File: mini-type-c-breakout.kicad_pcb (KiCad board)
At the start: 2 copper layers, 11 parts, among them J0 TYPE-C-31-M12_13_EDITED, J1 ConnectionPoint, J2 ConnectionPoint, J3 ConnectionPoint, J4 ConnectionPoint, J5 ConnectionPoint, J6 ConnectionPoint, J7 ConnectionPoint, J8 ConnectionPoint

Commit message: v1.0a complete
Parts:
- removed J1, J2, J3, J4, J5, J6, J7, J8: ConnectionPoint, TestPoint:TestPoint_THTPad_1.0x1.0mm_Drill0.5mm
- added D+: Conn_01x01, TestPoint:TestPoint_Pad_1.0x1.0mm, F.Cu at (281.0, 163.6)
- added D-: Conn_01x01, TestPoint:TestPoint_Pad_1.0x1.0mm, F.Cu at (279.6, 163.6)
- added GND: Conn_01x01, TestPoint:TestPoint_Pad_1.0x1.0mm, F.Cu at (277.3, 163.6)
- added VCC: Conn_01x01, TestPoint:TestPoint_Pad_1.0x1.0mm, F.Cu at (283.3, 163.6)
- J0: footprint mini-general-tweaks:TYPE-C-31-M-12-No-SHIELD -> mini-general-tweaks:HRO-TYPE-C-No-SHIELD
- R0, R1: moved to B.Cu
- moved J0 47.6 mm to (280.3, 160.3)
- moved R0 38.2 mm to (278.2, 163.5)
- moved R1 35.3 mm to (282.5, 163.5), turned to 180 degrees
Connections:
- net CC1 renamed Net-(J0-Pad4)
- net CC2 renamed Net-(J0-Pad10)
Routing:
- net VCC: track 0.00 -> 11.1 mm, vias 0 -> 2
- net GND: track 0.00 -> 6.64 mm, vias 0 -> 2
- net Net-(J0-Pad4): track 0.00 -> 4.21 mm, vias 0 -> 1
- net Net-(J0-Pad10): track 0.00 -> 3.79 mm, vias 0 -> 1
- net USB_D+: track 5.05 -> 7.36 mm, vias 0 -> 2
- net USB_D-: track 6.85 -> 7.54 mm
- added copper zone on B.Cu, net GND
- added copper zone on F.Cu, net GND
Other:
- board outline added: 7.6 x 4.8 mm
- board text added: "Non-standard Type C Breakout Board"

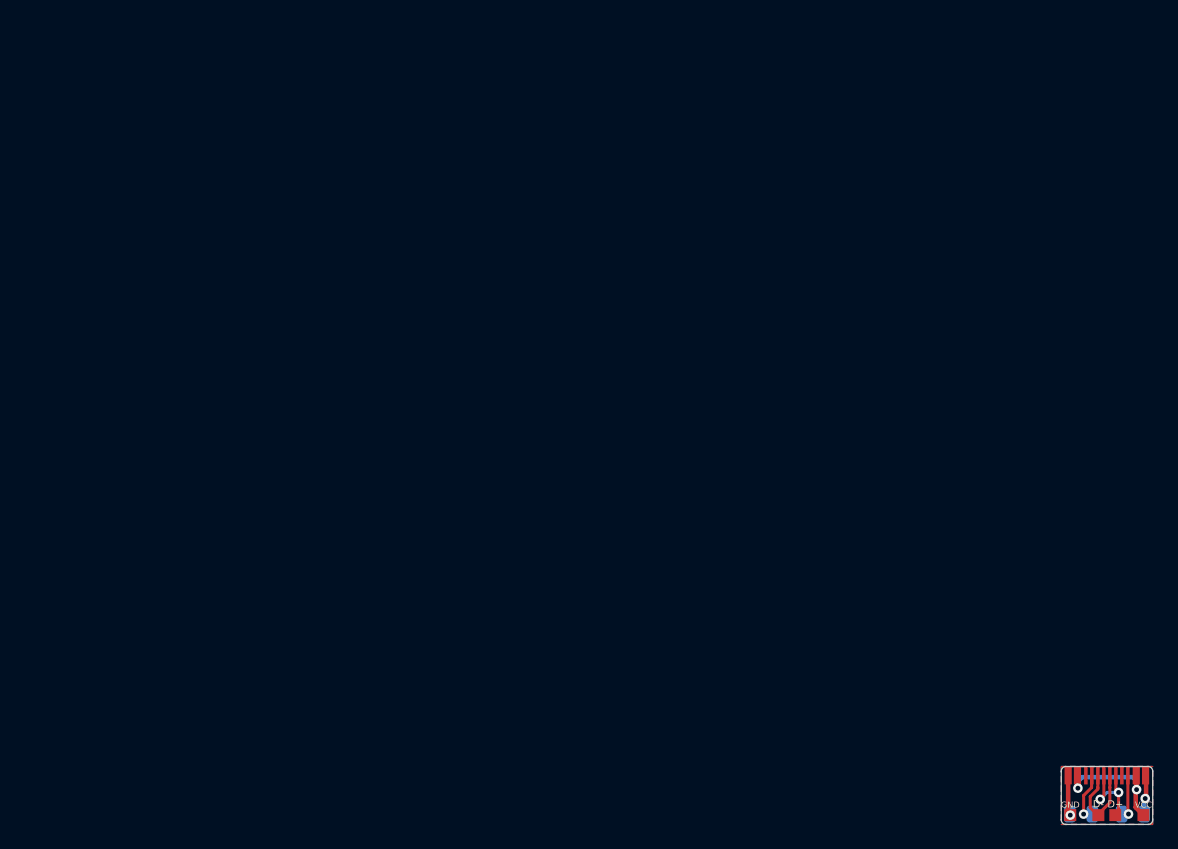
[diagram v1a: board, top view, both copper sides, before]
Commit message: Many tweaks, additions, etc.
Added licensing, tweaked PCB silkscreen, added logos to schematic, tweaked schematic layout, etc.
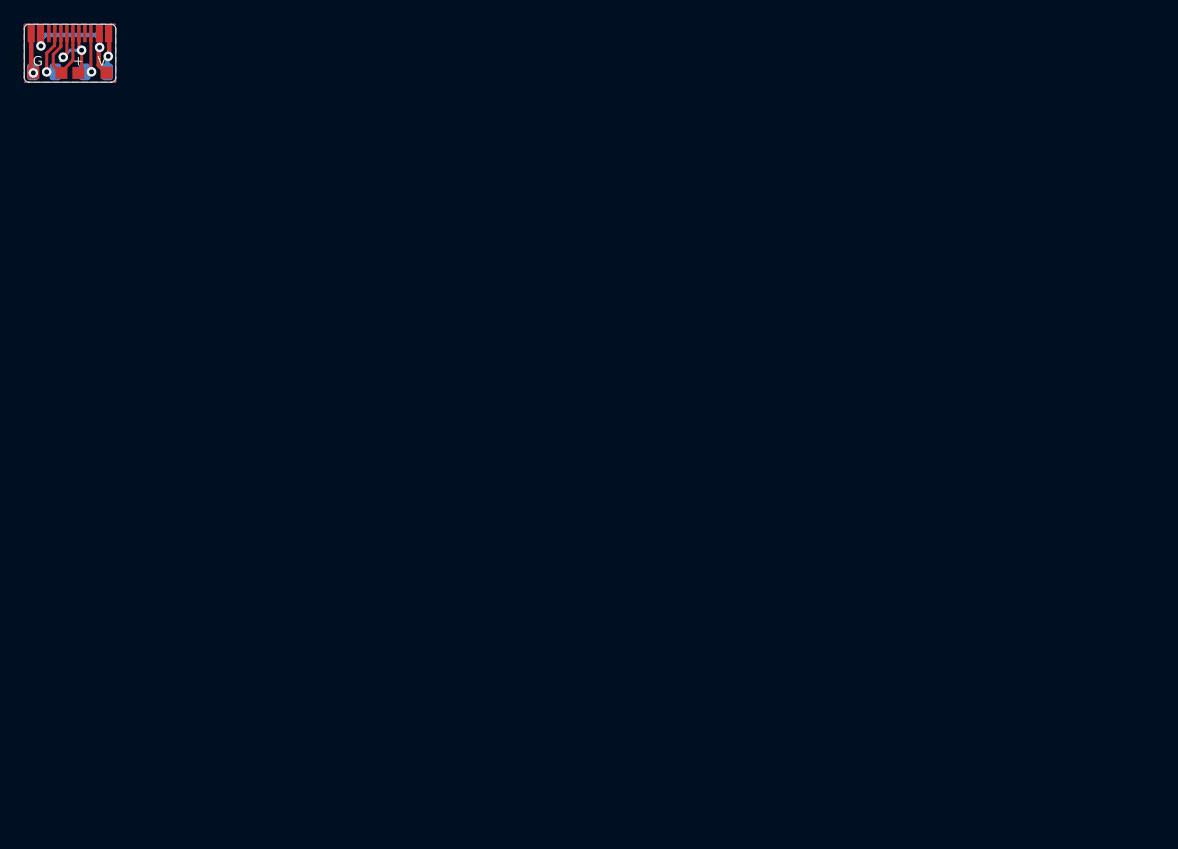
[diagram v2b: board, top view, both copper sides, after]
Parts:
- removed GND: Conn_01x01, TestPoint:TestPoint_Pad_1.0x1.0mm
- added G: Conn_01x01, TestPoint:TestPoint_Pad_1.0x1.0mm, F.Cu at (190.8, 101.8)
- moved + 106.3 mm to (194.6, 101.8)
- moved J0 106.3 mm to (193.9, 98.5)
- moved R0 106.3 mm to (191.7, 101.7)
- moved R1 106.3 mm to (196.1, 101.7)
- moved - 106.3 mm to (193.2, 101.8)
- moved V 106.3 mm to (196.9, 101.8)
- renumbered D+ to +, D- to -, VCC to V
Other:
- board text added: "Non-Standard!"
- board text removed: "Non-standard Type C Breakout Board"
